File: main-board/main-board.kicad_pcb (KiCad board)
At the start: 2 copper layers, 161.8 x 100 mm, 61 parts, among them J1 INPUT, J2 NC1, J3 OUTPUT, J4 Conn_01x03_Pin, J5 COM, J6 INPUT_DEBUG, J7 NC__DEBUG, J8 OUTPUT_DEBUG, SW1 SW_SPST, SW2 Power Switch A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

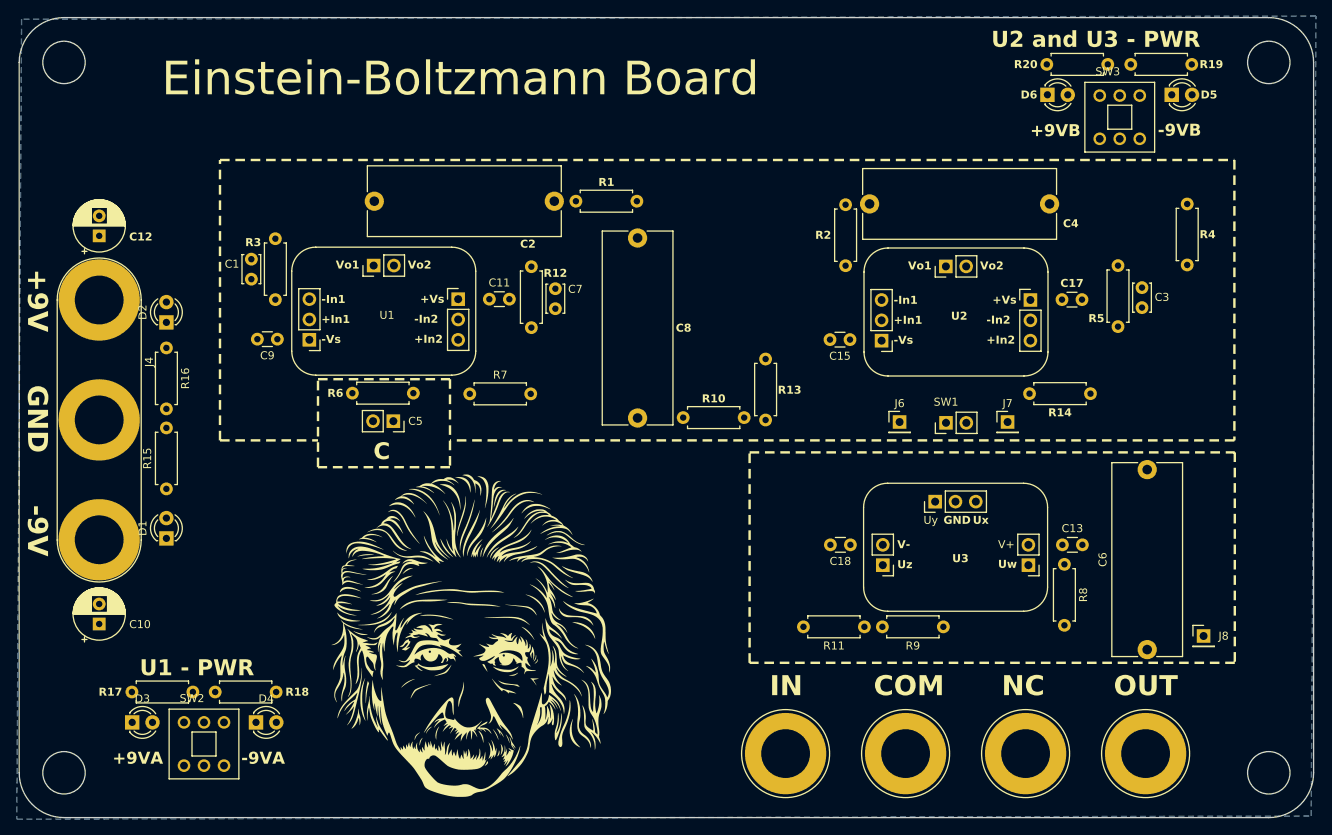
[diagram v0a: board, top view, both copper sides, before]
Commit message: Finishes Component displacement
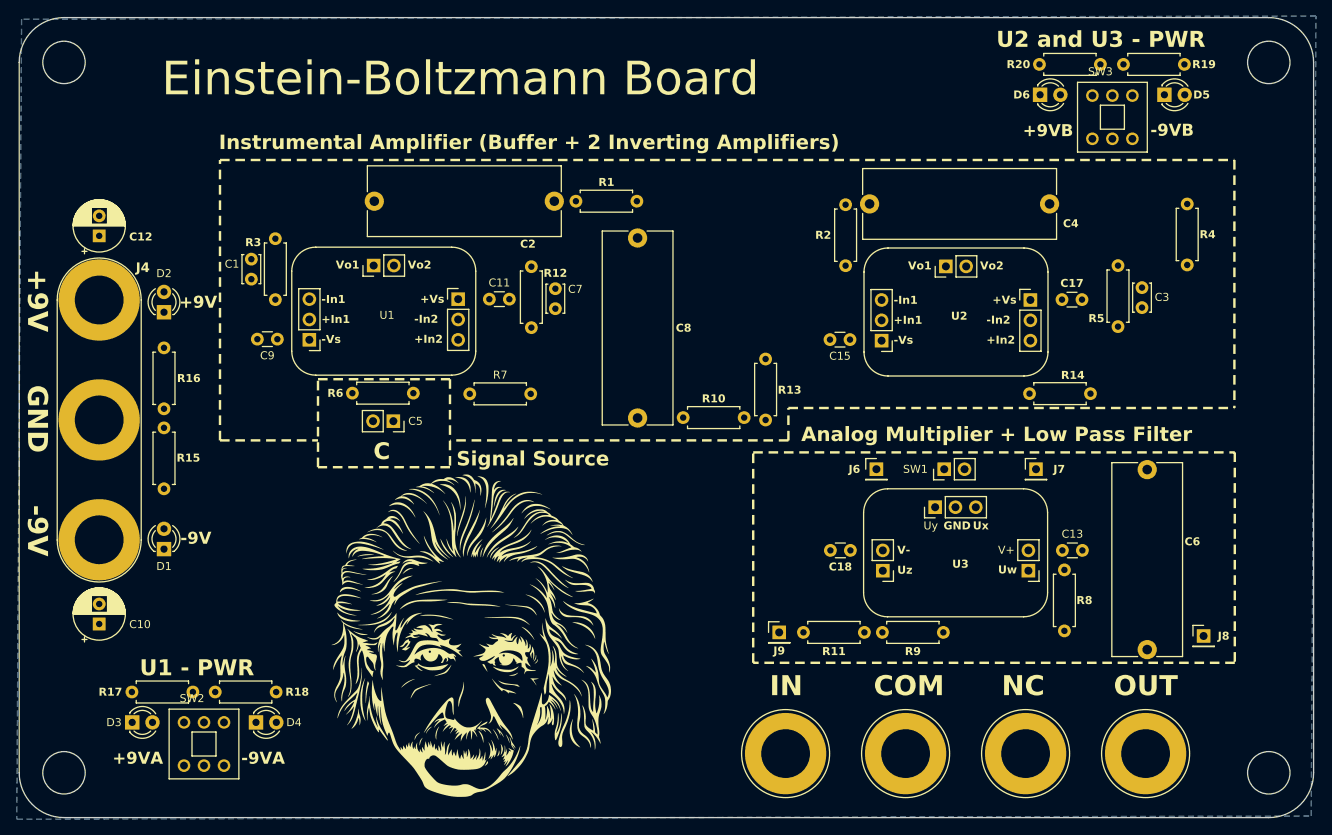
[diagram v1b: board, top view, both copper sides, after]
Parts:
- added G***: LOGO, LOGO, B.Cu at (115.0, 133.8)
- added J9: COM_DEBUG, Connector_PinHeader_2.54mm:PinHeader_1x01_P2.54mm_Vertical, F.Cu at (155.0, 130.8)
- moved J7 6.88 mm to (187.1, 110.5)
- moved J6 6.57 mm to (167.2, 110.5)
- moved SW1 5.80 mm to (175.6, 110.5)
- moved D1 1.37 mm to (78.1, 120.4)
- moved D2 1.30 mm to (78.1, 90.8)
- moved D5 0.92 mm to (203.2, 63.6)
- moved D6 0.92 mm to (187.6, 63.6)
- moved R19 0.92 mm to (205.7, 59.9)
- moved R20 0.92 mm to (187.5, 59.9)
- moved SW3 0.92 mm to (194.2, 63.8)
- moved R8 0.70 mm to (190.7, 123.0)
- moved U3 0.70 mm to (167.9, 123.1)
- moved C13 0.69 mm to (190.4, 120.6)
- moved C18 0.69 mm to (163.9, 120.6)
- moved R11 0.69 mm to (165.7, 130.8)
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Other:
- board text added: "Analog Multiplier + Low Pass Filter"
- board text added: "Instrumental Amplifier (Buffer + 2 Inverting Amplifiers)"
- board text added: "Signal Source"

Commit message: Done Routing with DRC 0 Errors and 0 Warnings
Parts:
- D1, D2, D3, D4, D5, D6: footprint LED_THT:LED_D3.0mm -> footprints:LED_D3.0mm
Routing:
- net -9V: track 0.00 -> 239.0 mm, vias 0 -> 2
- net +9V: track 0.00 -> 229.1 mm, vias 0 -> 2
- net +9VB: track 0.00 -> 124.0 mm
- net -9VB: track 0.00 -> 117.7 mm
- net /w_input: track 0.00 -> 101.9 mm
- net +9VA: track 0.00 -> 81.9 mm, vias 0 -> 2
- net -9VA: track 0.00 -> 65.4 mm
- net /w_nc: track 0.00 -> 52.8 mm
- net /w12: track 0.00 -> 37.6 mm
- net /w7: track 0.00 -> 35.7 mm
- net /w1: track 0.00 -> 35.3 mm, vias 0 -> 2
- net /w4: track 0.00 -> 34.3 mm
- net /w_out: track 0.00 -> 32.2 mm
- net /w8: track 0.00 -> 27.0 mm
- net /w3: track 0.00 -> 26.5 mm
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
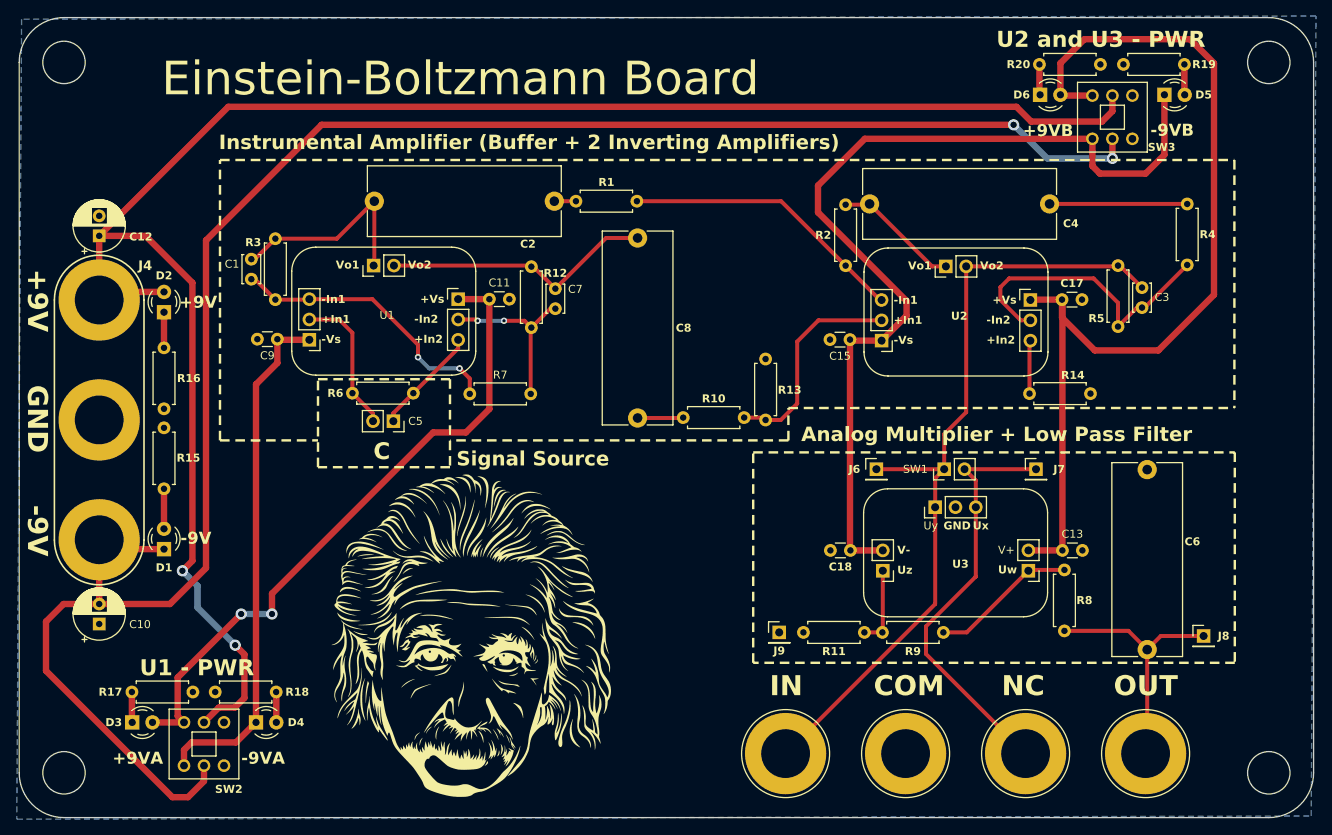
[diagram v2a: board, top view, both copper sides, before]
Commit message: Adds upper ground plane and via stitches the board
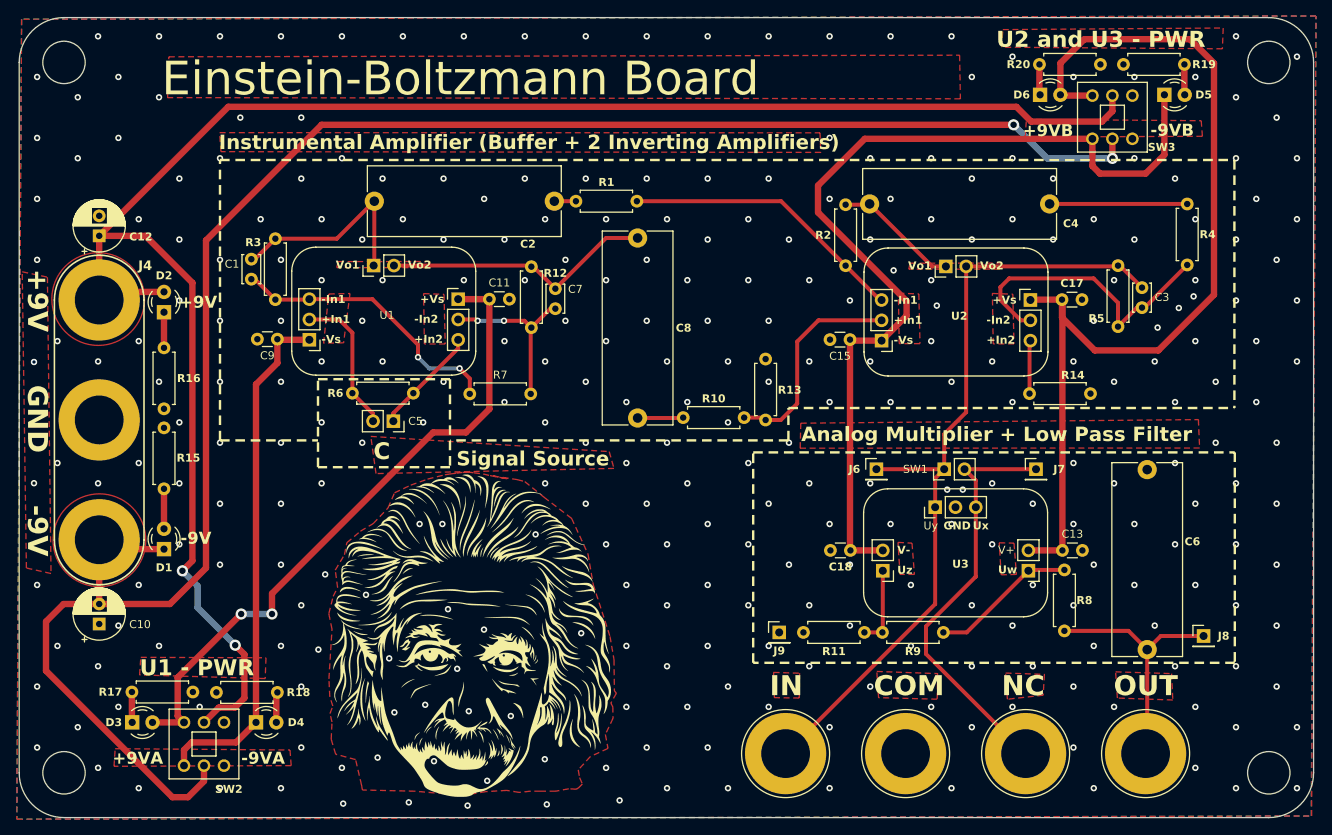
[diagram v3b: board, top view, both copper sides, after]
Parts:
- moved R18 0.16 mm to (92.3, 138.3)
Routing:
- net GND: vias 0 -> 312
- added copper zone on F.Cu, net (none)
- added copper zone on F.Cu, net GND
